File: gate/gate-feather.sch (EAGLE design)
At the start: 32 parts, among them J1 1X21X02-BIG, U1 SN75468

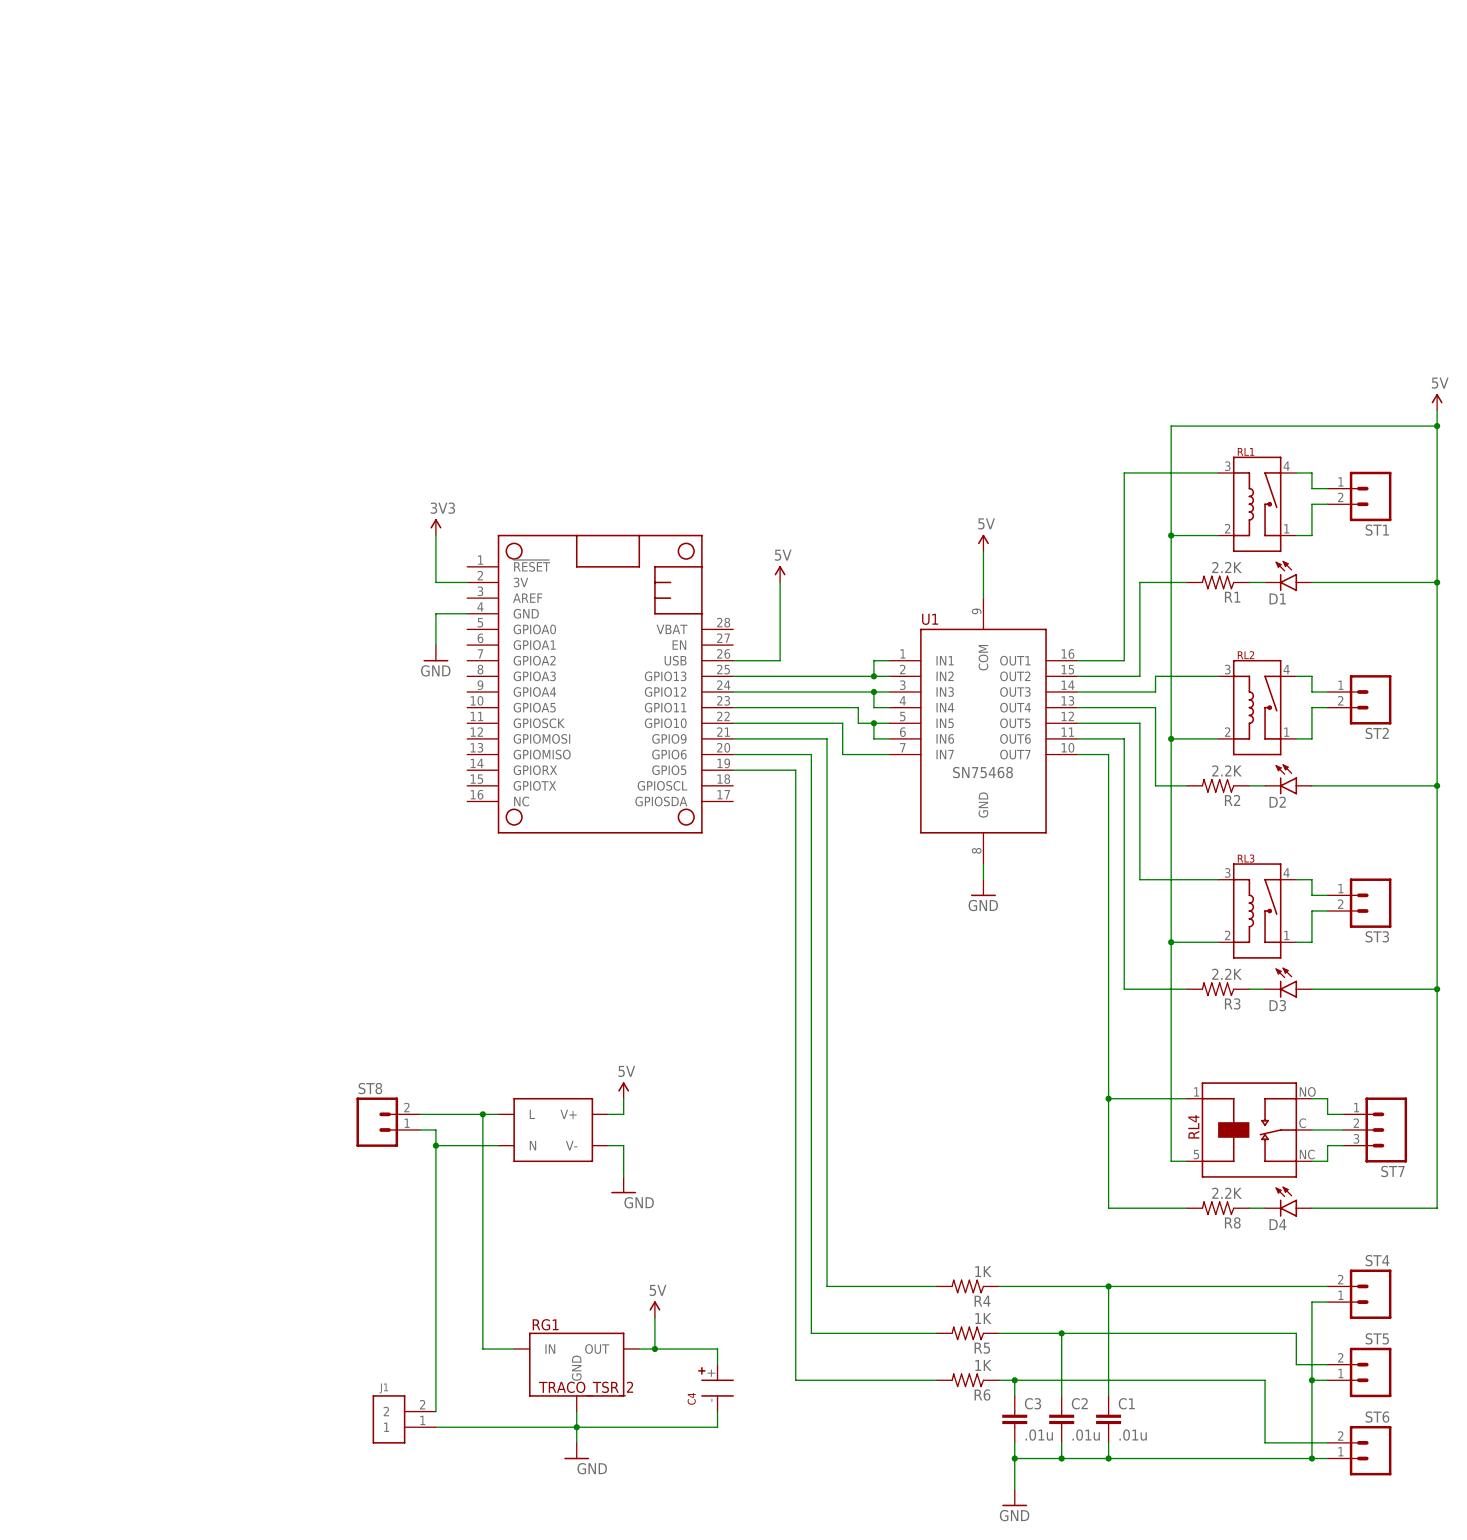
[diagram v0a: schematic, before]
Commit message: New argon and feather boards
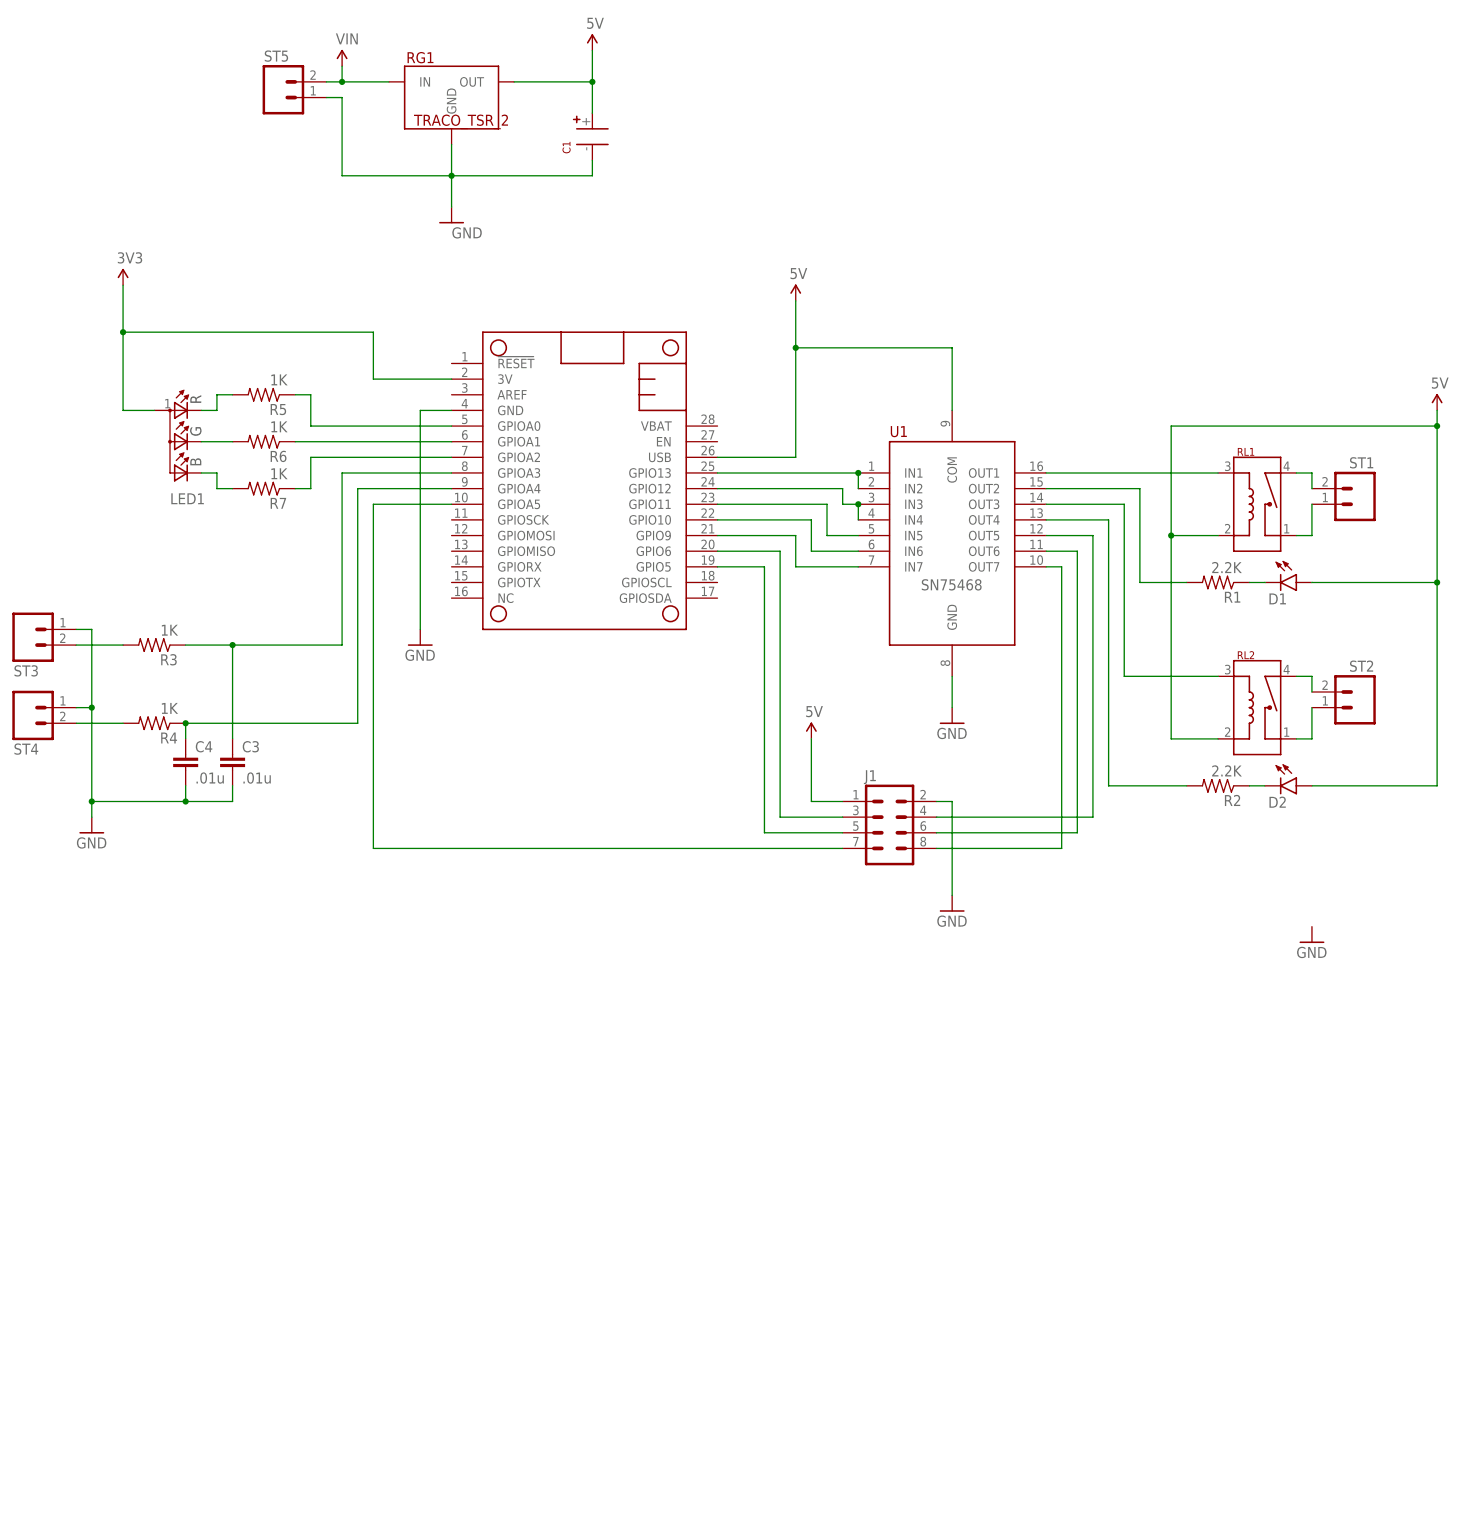
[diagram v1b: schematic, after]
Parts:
- removed C2: .01u, SparkFun-Capacitors:CAP0603-CAP
- removed D3, D4: (no value), SparkFun-LED:LED0603
- removed MS2: FEATHERWING_NODIM, adafruit:FEATHERWING_NODIM
- removed PWR1: IRM_03_PS_3W, Puffin:IRM_03_PS_3W
- removed R8: 2.2K, SparkFun-Resistors:RESISTOR0603
- removed RL3: HE3600_RELAY, Puffin:HE3600_RELAY
- removed RL4: G2RL_SPDT, Puffin:G2RL_SPDT
- removed ST6, ST8: (no value), Puffin:SCREWTERM_2
- removed ST7: (no value), Puffin:SCREWTERM_3
- added LED1: LED-RGB-CREE-SMD, SomUSB1:LED-RGB-CREE-SMD
- added MS1: FEATHERWING_NODIM, adafruit:FEATHERWING_NODIM
- added R7: 1K, SparkFun-Resistors:RESISTOR0603
- C1: value .01u -> (none); device SparkFun-Capacitors:CAP0603-CAP -> Puffin:CAPACITOR-AXIAL10X25
- C4: value (none) -> .01u; device Puffin:CAPACITOR-AXIAL10X25 -> SparkFun-Capacitors:CAP0603-CAP
- J1: value 1X21X02-BIG -> (none); device Puffin:1X21X02-BIG -> SparkFun-Connectors:M04X2
- R3: value 2.2K -> 1K
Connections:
- removed net 3V: MS2.3V
- removed net IN: PWR1.L, RG1.IN, ST8.2
- removed net N$14: RL3.C2, ST3.1
- removed net RC: RL4.C, ST7.2
- removed net RNC: RL4.NC, ST7.3
- removed net RNO: RL4.NO, ST7.1
- new net 3V3: LED1.A, MS1.3V
- new net N$21: MS1.GPIO10, U1.IN6
- new net N$24: J1.5, MS1.GPIO5
- new net N$25: J1.7, MS1.GPIOA5
- new net N$8: MS1.GPIO11, U1.IN5
- new net VIN: RG1.IN, ST5.2
- net 5V: now also C1.+, J1.1, MS1.USB; no longer C4.+, D3.A, D4.A, MS2.USB, PWR1.V+, RL3.R1, RL4.P$2
- net GND: now also C1.-, C4.2, J1.2, MS1.GND, ST3.1; no longer C1.2, C2.2, C4.-, J1.1, MS2.GND, PWR1.V-, ST6.1
- net L5: now also J1.4; no longer RL3.R2
- net L6: now also J1.6; no longer R3.2
- net L7: now also J1.8; no longer R8.2, RL4.P$1
- net N$10: now also LED1.R, R5.2; no longer RL3.C1, ST3.2
- net N$11: now also LED1.G, R6.2; no longer MS2.GPIO10, U1.IN7
- net N$12: now also LED1.B, R7.2; no longer C3.1, R6.1, ST6.2
- net N$13: now also ST1.1; no longer ST1.2
- net N$15: now also MS1.GPIOA1, R6.1; no longer D3.C, R3.1
- net N$16: now also MS1.GPIOA0, R5.1; no longer MS2.GPIO9, R4.2
- net N$17: now also R4.2, ST4.2; no longer MS2.GPIO6, R5.2
- net N$18: now also R3.2, ST3.2; no longer MS2.GPIO5, R6.2
- net N$19: now also MS1.GPIOA2, R7.1; no longer MS2.GPIO11, U1.IN5, U1.IN6
- net N$2: now also ST1.2; no longer ST1.1
- net N$20: now also J1.3, MS1.GPIO6; no longer J1.2, PWR1.N, ST8.1
- net N$23: now also MS1.GPIO9, U1.IN7; no longer D4.C, R8.1
- net N$26: now also MS1.GPIO13; no longer MS2.GPIO13
- net N$27: now also MS1.GPIO12; no longer MS2.GPIO12
- net N$31: now also C3.1, MS1.GPIOA3, R3.1; no longer C1.1, R4.1, ST4.2
- net N$4: now also ST2.2; no longer ST2.1
- net N$7: now also C4.1, MS1.GPIOA4, R4.1; no longer C2.1, R5.1, ST5.2
- net N$9: now also ST2.1; no longer ST2.2
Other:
- moved on the sheet: C3, R3, R4, R5, R6, RG1, ST1, ST2, ST3, ST4, ST5, U1
